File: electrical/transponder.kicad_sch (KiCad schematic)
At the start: 4 parts

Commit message: Interim check-in. Not sure what I was doing.
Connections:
- net ADSB_SERIAL_GND: now also GTX45R.P3251_50 (RS-232_GND_3); no longer GTX45R.P3252_15 (RS-232_GND_4)
- net ADSB_SERIAL_IN: now also GTX45R.P3251_29 (RS-232_IN_3); no longer GTX45R.P3252_10 (RS-232_IN_4)
- net ADSB_SERIAL_OUT: now also GTX45R.P3251_7 (RS-232_OUT_3); no longer GTX45R.P3252_5 (RS-232_OUT_4)
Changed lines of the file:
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@@
+    (stroke (width 0) (type default))
+  )
+  (wire (pts (xy 77.47 106.68) (xy 86.36 106.68))
     (stroke (width 0) (type default))
   )
   (wire (pts (xy 77.47 86.36) (xy 104.14 86.36))
-    (stroke (width 0) (type default))
-  )
-  (wire (pts (xy 77.47 147.32) (xy 86.36 147.32))
     (stroke (width 0) (type default))
   )
@@
     (stroke (width 0) (type default))
   )
-  (wire (pts (xy 77.47 144.78) (xy 86.36 144.78))
-    (stroke (width 0) (type default))
-  )
   (wire (pts (xy 130.81 124.46) (xy 130.81 132.08))
     (stroke (width 0) (type default))
@@
     (stroke (width 0) (type default))
   )
+  (wire (pts (xy 77.47 101.6) (xy 86.36 101.6))
+    (stroke (width 0) (type default))
+  )
   (wire (pts (xy 125.73 119.38) (xy 134.62 119.38))
     (stroke (width 0) (type default))
@@
     (stroke (width 0) (type default))
   )
-  (wire (pts (xy 77.47 149.86) (xy 86.36 149.86))
+  (wire (pts (xy 77.47 104.14) (xy 86.36 104.14))
     (stroke (width 0) (type default))
   )
@@
     (stroke (width 0) (type default))
   )
-  (text "To GDU450\nConnext Fmt 1\nPage 24-35" (at 114.3 149.86 0)
+  (text_box "Airdata should be RS2321"
+    (at 144.78 81.915 0) (size 16.51 6.985)
+    (stroke (width 0) (type default))
+    (fill (type none))
+    (effects (font (size 1.27 1.27)) (justify left top))
+  )
+  (text_box "Believe RS232 2 is from GPS 20"
+    (at 89.535 92.71 0) (size 31.75 5.08)
+    (stroke (width 0) (type default))
+    (fill (type none))
+    (effects (font (size 1.27 1.27)) (justify left top))
+  )
+  (text "To GDU450\nConnext Fmt 1\nPage 24-35" (at 114.3 106.68 0)
     (effects (font (size 1.27 1.27)) (justify left bottom))
   )
@@
     (effects (font (size 1.27 1.27)) (justify left))
   )
-  (hierarchical_label "ADSB_SERIAL_OUT" (shape output) (at 86.36 144.78 0) (fields_autoplaced)
+  (hierarchical_label "ADSB_SERIAL_OUT" (shape output) (at 86.36 101.6 0) (fields_autoplaced)
     (effects (font (size 1.27 1.27)) (justify left))
   )
@@
     (effects (font (size 1.27 1.27)) (justify left))
   )
-  (hierarchical_label "ADSB_SERIAL_IN" (shape input) (at 86.36 147.32 0) (fields_autoplaced)
+  (hierarchical_label "ADSB_SERIAL_IN" (shape input) (at 86.36 104.14 0) (fields_autoplaced)
     (effects (font (size 1.27 1.27)) (justify left))
   )
@@
     (effects (font (size 1.27 1.27)) (justify left))
   )
-  (hierarchical_label "ADSB_SERIAL_GND" (shape passive) (at 86.36 149.86 0) (fields_autoplaced)
+  (hierarchical_label "ADSB_SERIAL_GND" (shape passive) (at 86.36 106.68 0) (fields_autoplaced)
     (effects (font (size 1.27 1.27)) (justify left))
   )

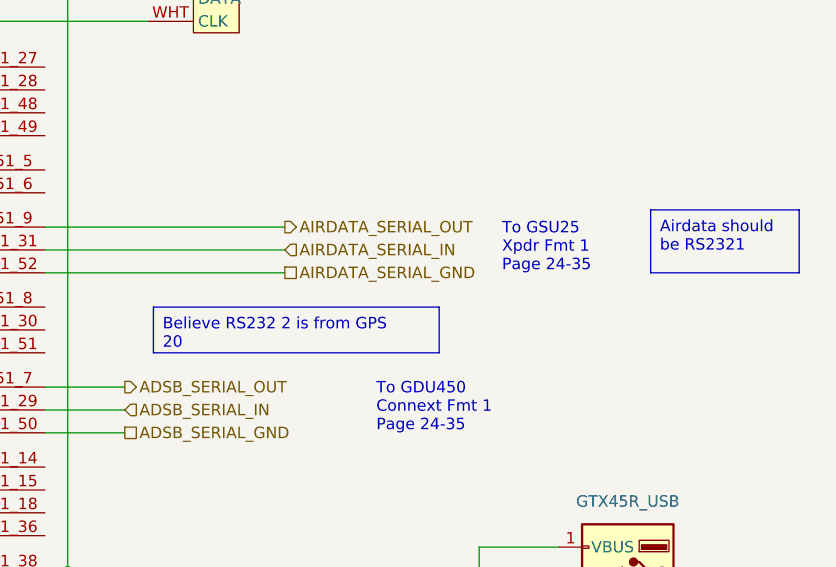
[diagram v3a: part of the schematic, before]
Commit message: Cleaned up power and smoke.
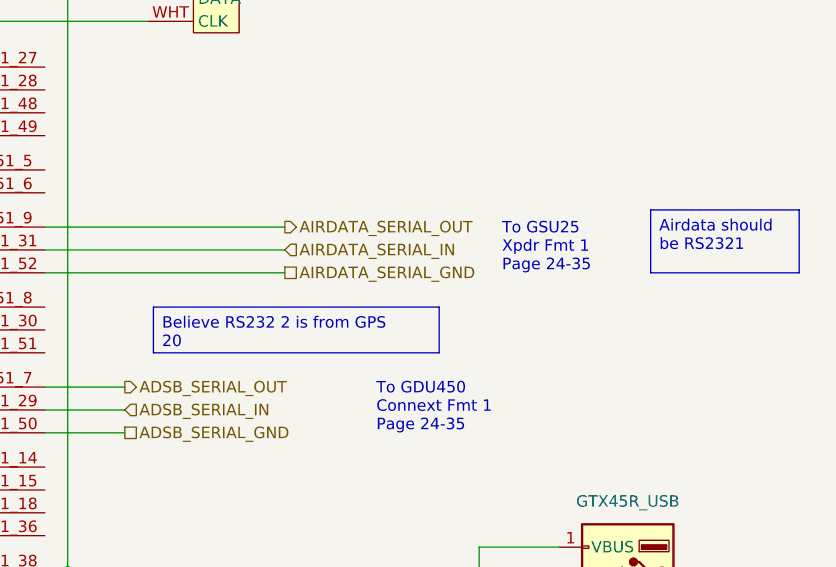
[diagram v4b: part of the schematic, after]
